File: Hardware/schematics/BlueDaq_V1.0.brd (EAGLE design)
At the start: 100 x 80 mm, 72 parts, among them IC1 MEGA8-AI, Q1 MMBT2222, Q2 MMBT2222, Q3 MMBT2222, Q4 MMBT2222, U1 MCP73831, U2 TPS61200, U3 BME280, U4 MIC5225-3.3, U5 MIC5219 5V, X1 USB-MICROB, X2 3.5mm, X4 3.5mm, Y1 16 mhz

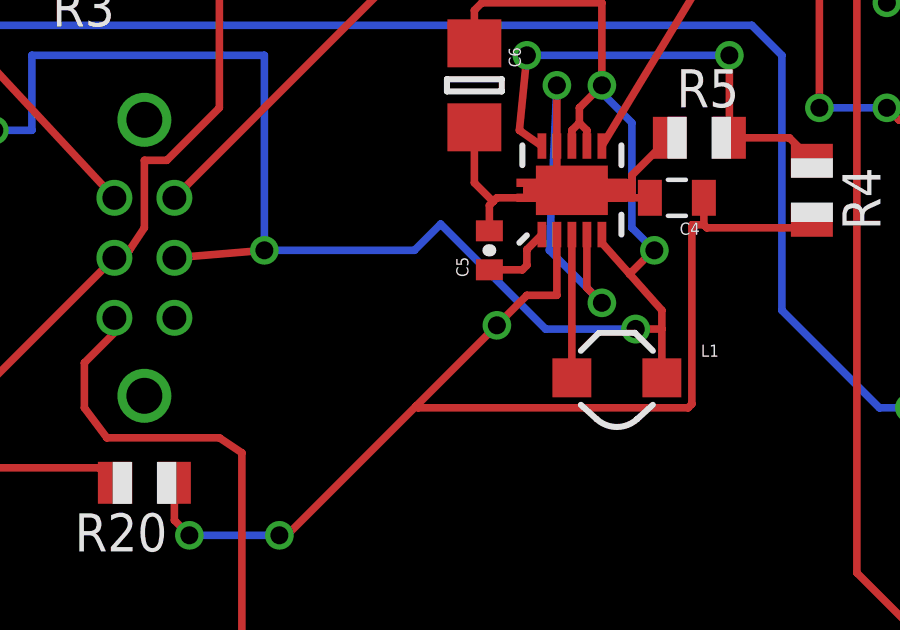
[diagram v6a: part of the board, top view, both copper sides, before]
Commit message: prettier, no DRC errors
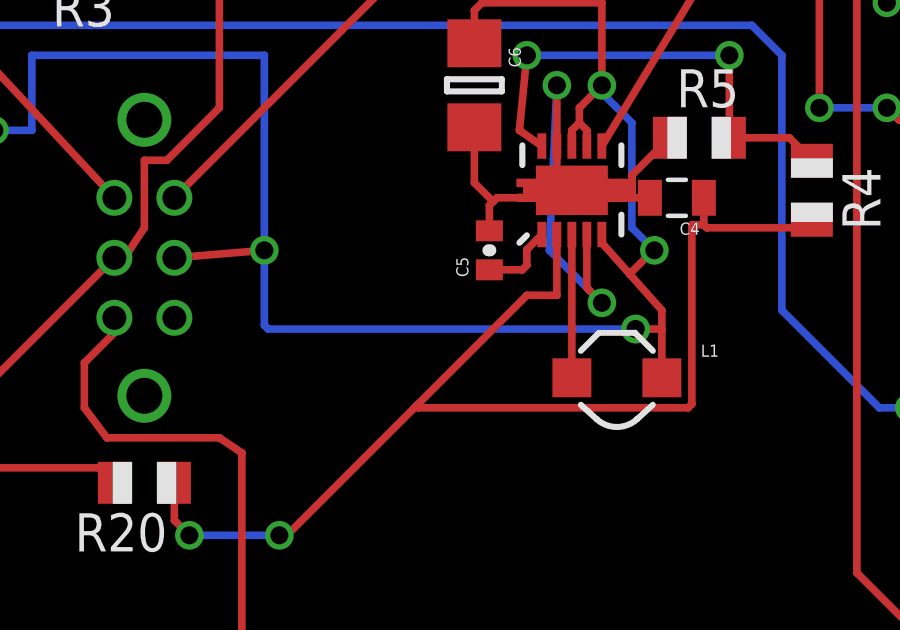
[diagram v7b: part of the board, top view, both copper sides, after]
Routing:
- net VBATT: track 75.8 -> 76.5 mm
- net N$20: vias 3 -> 2
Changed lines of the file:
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@@
 <wire x1="20.75" y1="22" x2="17.75" y2="21.75" width="0.254" layer="1"/>
 <wire x1="33.125" y1="19.375" x2="34" y2="19.375" width="0.254" layer="1"/>
-<wire x1="30.125" y1="19.375" x2="33.125" y2="19.375" width="0.254" layer="16"/>
-<wire x1="26.625" y1="22.875" x2="30.125" y2="19.375" width="0.254" layer="16"/>
+<wire x1="20.875" y1="19.375" x2="33.125" y2="19.375" width="0.254" layer="16"/>
 <via x="33.125" y="19.375" extent="1-16" drill="0.6096"/>
-<wire x1="20.75" y1="22" x2="25.75" y2="22" width="0.254" layer="16"/>
-<wire x1="25.75" y1="22" x2="26.625" y2="22.875" width="0.254" layer="16"/>
+<wire x1="20.75" y1="22" x2="20.75" y2="19.5" width="0.254" layer="16"/>
+<wire x1="20.75" y1="19.5" x2="20.875" y2="19.375" width="0.254" layer="16"/>
 <via x="20.75" y="22" extent="1-16" drill="0.6" diameter="0.254"/>
 <wire x1="27.75" y1="28.9" x2="27.75" y2="30" width="0.254" layer="1"/>
@@
 <wire x1="21.25" y1="12.5" x2="21.5" y2="12.5" width="0.254" layer="1"/>
 <wire x1="21.5" y1="12.5" x2="25.8125" y2="16.8125" width="0.254" layer="1"/>
-<wire x1="25.8125" y1="16.8125" x2="28.5" y2="19.5" width="0.254" layer="1"/>
-<wire x1="28.5" y1="19.5" x2="29.5" y2="20.5" width="0.254" layer="1"/>
+<wire x1="25.8125" y1="16.8125" x2="29.5" y2="20.5" width="0.254" layer="1"/>
 <wire x1="29.5" y1="20.5" x2="30.5" y2="20.5" width="0.254" layer="1"/>
 <wire x1="30.5" y1="20.5" x2="30.5" y2="22.525" width="0.254" layer="1"/>
@@
 <wire x1="25.875" y1="16.75" x2="34.875" y2="16.75" width="0.254" layer="1"/>
 <wire x1="25.875" y1="16.75" x2="25.8125" y2="16.8125" width="0.254" layer="1"/>
-<via x="28.5" y="19.5" extent="1-16" drill="0.6" diameter="0.254"/>
 <via x="18.25" y="12.5" extent="1-16" drill="0.6" diameter="0.254"/>
 <via x="21.25" y="12.5" extent="1-16" drill="0.6" diameter="0.254"/>

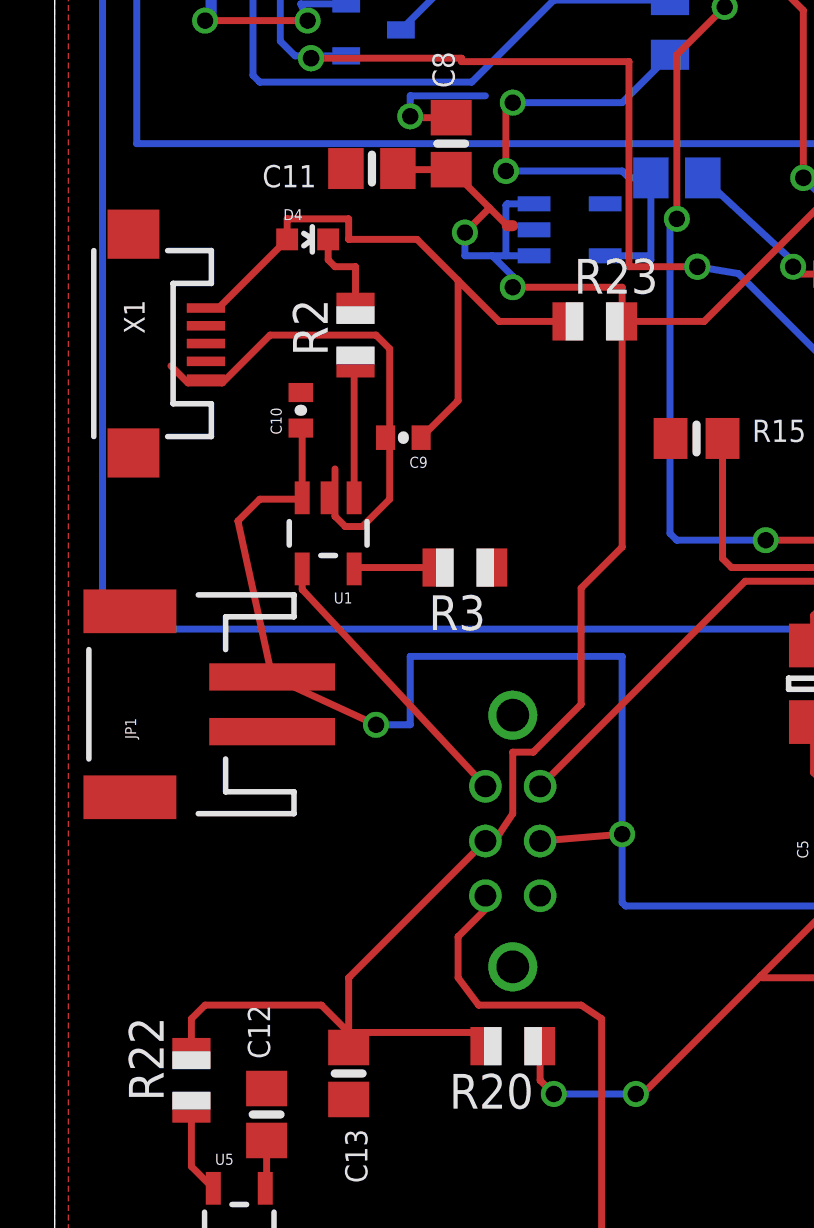
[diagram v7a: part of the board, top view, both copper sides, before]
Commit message: made vcc line beefier
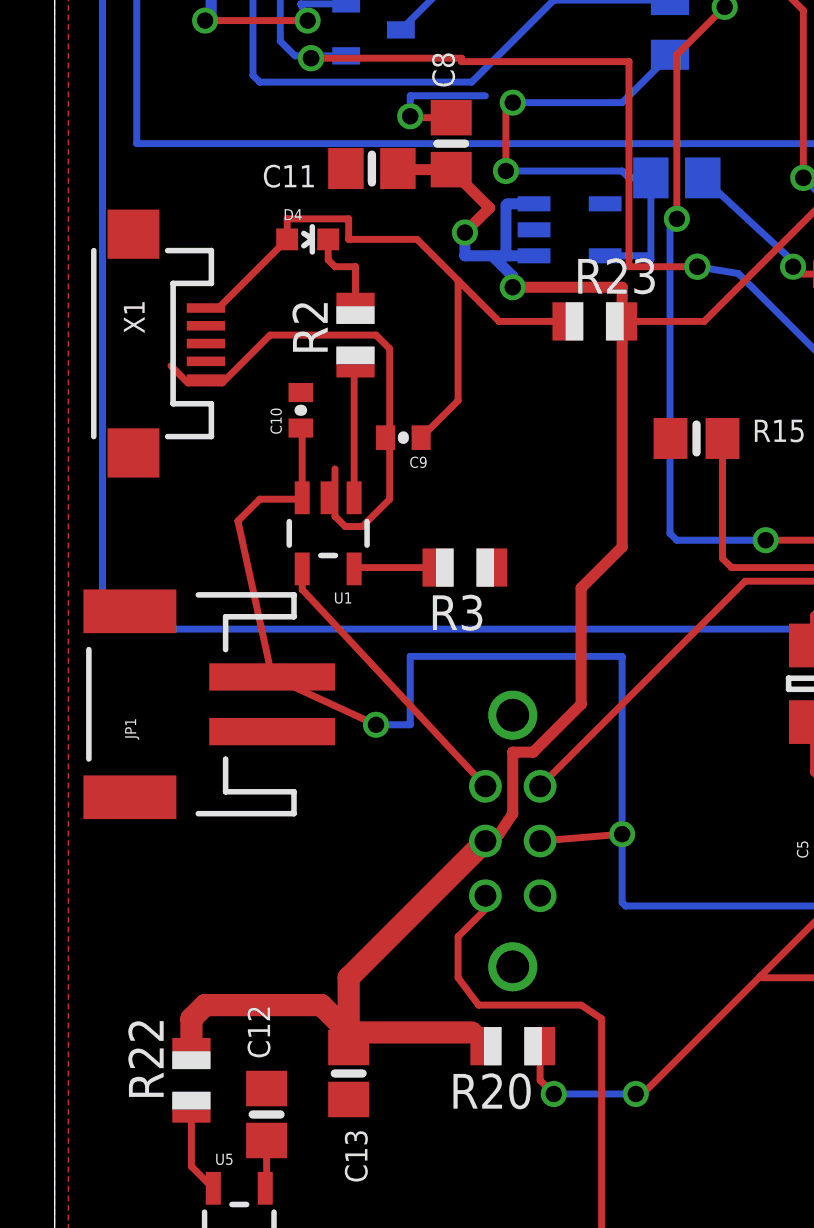
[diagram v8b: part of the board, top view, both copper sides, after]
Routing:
- net VCC: track 201.4 -> 200.3 mm
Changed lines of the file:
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@@
 <contactref element="R22" pad="2"/>
 <contactref element="R23" pad="2"/>
-<wire x1="5" y1="14" x2="5" y2="15.25" width="0.254" layer="1"/>
-<wire x1="5" y1="15.25" x2="5.5" y2="15.75" width="0.254" layer="1"/>
-<wire x1="5.5" y1="15.75" x2="9.75" y2="15.75" width="0.254" layer="1"/>
-<wire x1="9.75" y1="15.75" x2="10.75" y2="14.75" width="0.254" layer="1"/>
-<wire x1="10.75" y1="14.75" x2="15.25" y2="14.75" width="0.254" layer="1"/>
+<wire x1="5" y1="14" x2="5" y2="15.25" width="0.8128" layer="1"/>
+<wire x1="5" y1="15.25" x2="5.5" y2="15.75" width="0.8128" layer="1"/>
+<wire x1="5.5" y1="15.75" x2="9.75" y2="15.75" width="0.8128" layer="1"/>
+<wire x1="9.75" y1="15.75" x2="10.75" y2="14.75" width="0.8128" layer="1"/>
+<wire x1="10.75" y1="14.75" x2="15.25" y2="14.75" width="0.8128" layer="1"/>
 <wire x1="15.25" y1="14.75" x2="15.75" y2="14.25" width="0.254" layer="1"/>
-<wire x1="10.75" y1="14.75" x2="10.75" y2="16.75" width="0.254" layer="1"/>
-<wire x1="10.75" y1="16.75" x2="15.75" y2="21.75" width="0.254" layer="1"/>
+<wire x1="10.75" y1="14.75" x2="10.75" y2="16.75" width="0.8128" layer="1"/>
+<wire x1="10.75" y1="16.75" x2="15.75" y2="21.75" width="0.8128" layer="1"/>
 <wire x1="12.55" y1="46.34" x2="12.59" y2="46.3" width="0.254" layer="1"/>
-<wire x1="12.59" y1="46.3" x2="14.5" y2="46.3" width="0.254" layer="1"/>
-<wire x1="16.75" y1="44.25" x2="16.55" y2="44.25" width="0.4064" layer="1"/>
-<wire x1="16.55" y1="44.25" x2="15.9" y2="44.9" width="0.254" layer="1"/>
-<wire x1="15.9" y1="44.9" x2="14.5" y2="46.3" width="0.254" layer="1"/>
-<wire x1="15.75" y1="21.75" x2="16.25" y2="22" width="0.254" layer="1"/>
-<wire x1="16.25" y1="22" x2="16.75" y2="22.75" width="0.254" layer="1"/>
-<wire x1="16.75" y1="22.75" x2="16.75" y2="25" width="0.254" layer="1"/>
+<wire x1="12.59" y1="46.3" x2="14.5" y2="46.3" width="0.4064" layer="1"/>
+<wire x1="15.9" y1="44.9" x2="14.5" y2="46.3" width="0.4064" layer="1"/>
+<wire x1="15.75" y1="21.75" x2="16.25" y2="22" width="0.4064" layer="1"/>
+<wire x1="16.25" y1="22" x2="16.75" y2="22.75" width="0.4064" layer="1"/>
+<wire x1="16.75" y1="22.75" x2="16.75" y2="25" width="0.4064" layer="1"/>
 <wire x1="10.75" y1="14.75" x2="10.75" y2="14.2" width="0.254" layer="1"/>
-<wire x1="16.75" y1="25" x2="17.5" y2="25" width="0.254" layer="1"/>
-<wire x1="17.5" y1="25" x2="19.25" y2="26.75" width="0.254" layer="1"/>
-<wire x1="19.25" y1="26.75" x2="19.25" y2="31" width="0.254" layer="1"/>
-<wire x1="19.25" y1="31" x2="20.75" y2="32.5" width="0.254" layer="1"/>
-<wire x1="20.75" y1="32.5" x2="20.75" y2="40.75" width="0.254" layer="1"/>
+<wire x1="16.75" y1="25" x2="17.5" y2="25" width="0.4064" layer="1"/>
+<wire x1="17.5" y1="25" x2="19.25" y2="26.75" width="0.4064" layer="1"/>
+<wire x1="19.25" y1="26.75" x2="19.25" y2="31" width="0.4064" layer="1"/>
+<wire x1="19.25" y1="31" x2="20.75" y2="32.5" width="0.4064" layer="1"/>
+<wire x1="20.75" y1="32.5" x2="20.75" y2="40.75" width="0.4064" layer="1"/>
 <wire x1="56.86" y1="62.13" x2="54.63" y2="62.13" width="0.254" layer="1"/>
 <wire x1="54.63" y1="62.13" x2="54.5" y2="62" width="0.254" layer="1"/>
@@
 <wire x1="53.75" y1="51" x2="42.75" y2="49" width="0.254" layer="16"/>
 <via x="42.75" y="49" extent="1-16" drill="0.6" diameter="0.254"/>
-<wire x1="17.5299" y1="43.15" x2="16.5" y2="43.15" width="0.254" layer="16"/>
-<wire x1="16.5" y1="43.15" x2="16" y2="43.15" width="0.254" layer="16"/>
-<wire x1="16" y1="43.15" x2="15" y2="43.15" width="0.254" layer="16"/>
-<wire x1="15" y1="43.15" x2="15" y2="44" width="0.254" layer="16"/>
-<via x="15" y="44" extent="1-16" drill="0.6" diameter="0.254" shape="octagon"/>
-<wire x1="15" y1="44" x2="15.9" y2="44.9" width="0.254" layer="1"/>
-<wire x1="17.5299" y1="45.05" x2="16.55" y2="45.05" width="0.254" layer="16"/>
+<wire x1="17.5299" y1="43.15" x2="16.5" y2="43.15" width="0.4064" layer="16"/>
+<wire x1="16.5" y1="43.15" x2="16" y2="43.15" width="0.4064" layer="16"/>
+<wire x1="16" y1="43.15" x2="15" y2="43.15" width="0.4064" layer="16"/>
+<wire x1="15" y1="43.15" x2="15" y2="44" width="0.4064" layer="16"/>
+<via x="15" y="44" extent="1-16" drill="0.6" diameter="0.4064"/>
+<wire x1="15" y1="44" x2="15.9" y2="44.9" width="0.4064" layer="1"/>
+<wire x1="17.5299" y1="45.05" x2="16.55" y2="45.05" width="0.4064" layer="16"/>
 <wire x1="16.55" y1="45.05" x2="16.5" y2="45" width="0.254" layer="16"/>
-<wire x1="16.5" y1="45" x2="16.5" y2="43.15" width="0.254" layer="16"/>
-<wire x1="20.75" y1="40.75" x2="20.75" y2="42" width="0.254" layer="1"/>
-<wire x1="20.75" y1="42" x2="16.75" y2="42" width="0.254" layer="1"/>
-<wire x1="16.75" y1="42" x2="16.75" y2="42.4" width="0.254" layer="16"/>
-<wire x1="16.75" y1="42.4" x2="16" y2="43.15" width="0.254" layer="16"/>
-<via x="16.75" y="42" extent="1-16" drill="0.6" diameter="0.254"/>
+<wire x1="16.5" y1="45" x2="16.5" y2="43.15" width="0.4064" layer="16"/>
+<wire x1="20.75" y1="40.75" x2="20.75" y2="42" width="0.4064" layer="1"/>
+<wire x1="20.75" y1="42" x2="16.75" y2="42" width="0.4064" layer="1"/>
+<wire x1="16.75" y1="42" x2="16.75" y2="42.4" width="0.4064" layer="16"/>
+<wire x1="16.75" y1="42.4" x2="16" y2="43.15" width="0.4064" layer="16"/>
+<via x="16.75" y="42" extent="1-16" drill="0.6" diameter="0.4064"/>
 <wire x1="42.75" y1="49" x2="42.75" y2="46.25" width="0.254" layer="1"/>
 <wire x1="42.75" y1="46.25" x2="41" y2="44.5" width="0.254" layer="16"/>
